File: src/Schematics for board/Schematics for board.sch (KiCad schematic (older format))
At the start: 1 part

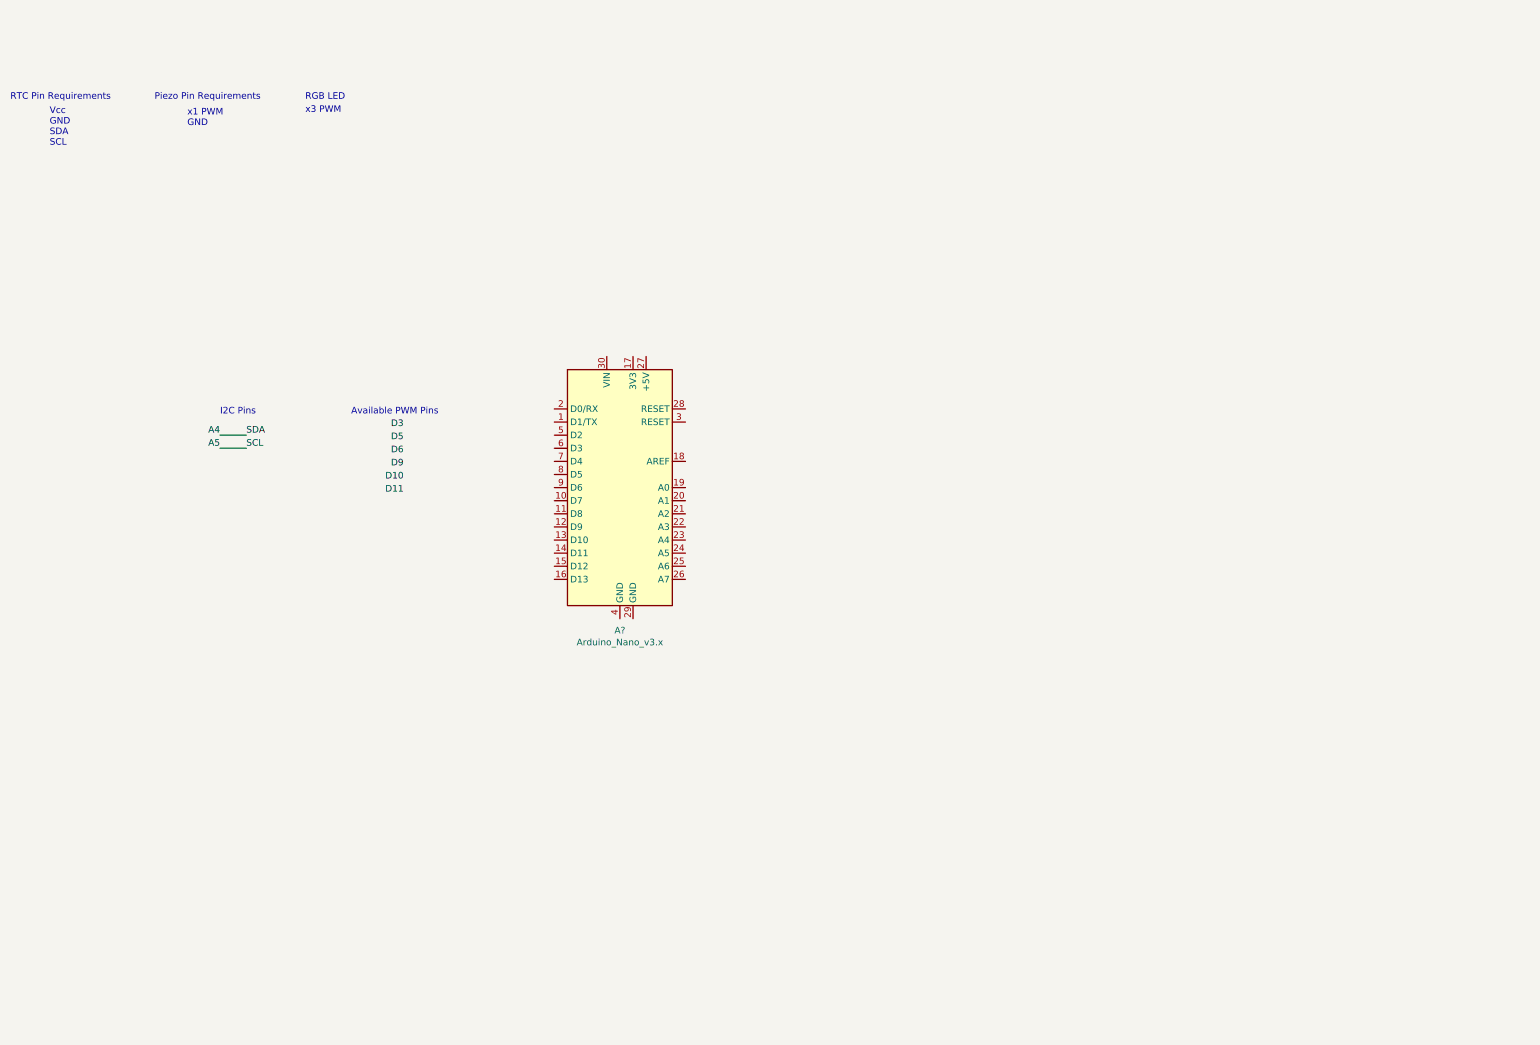
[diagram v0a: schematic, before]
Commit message: Rev1.0 of Board layout
Rev1 of how each part is going to be connected in out board
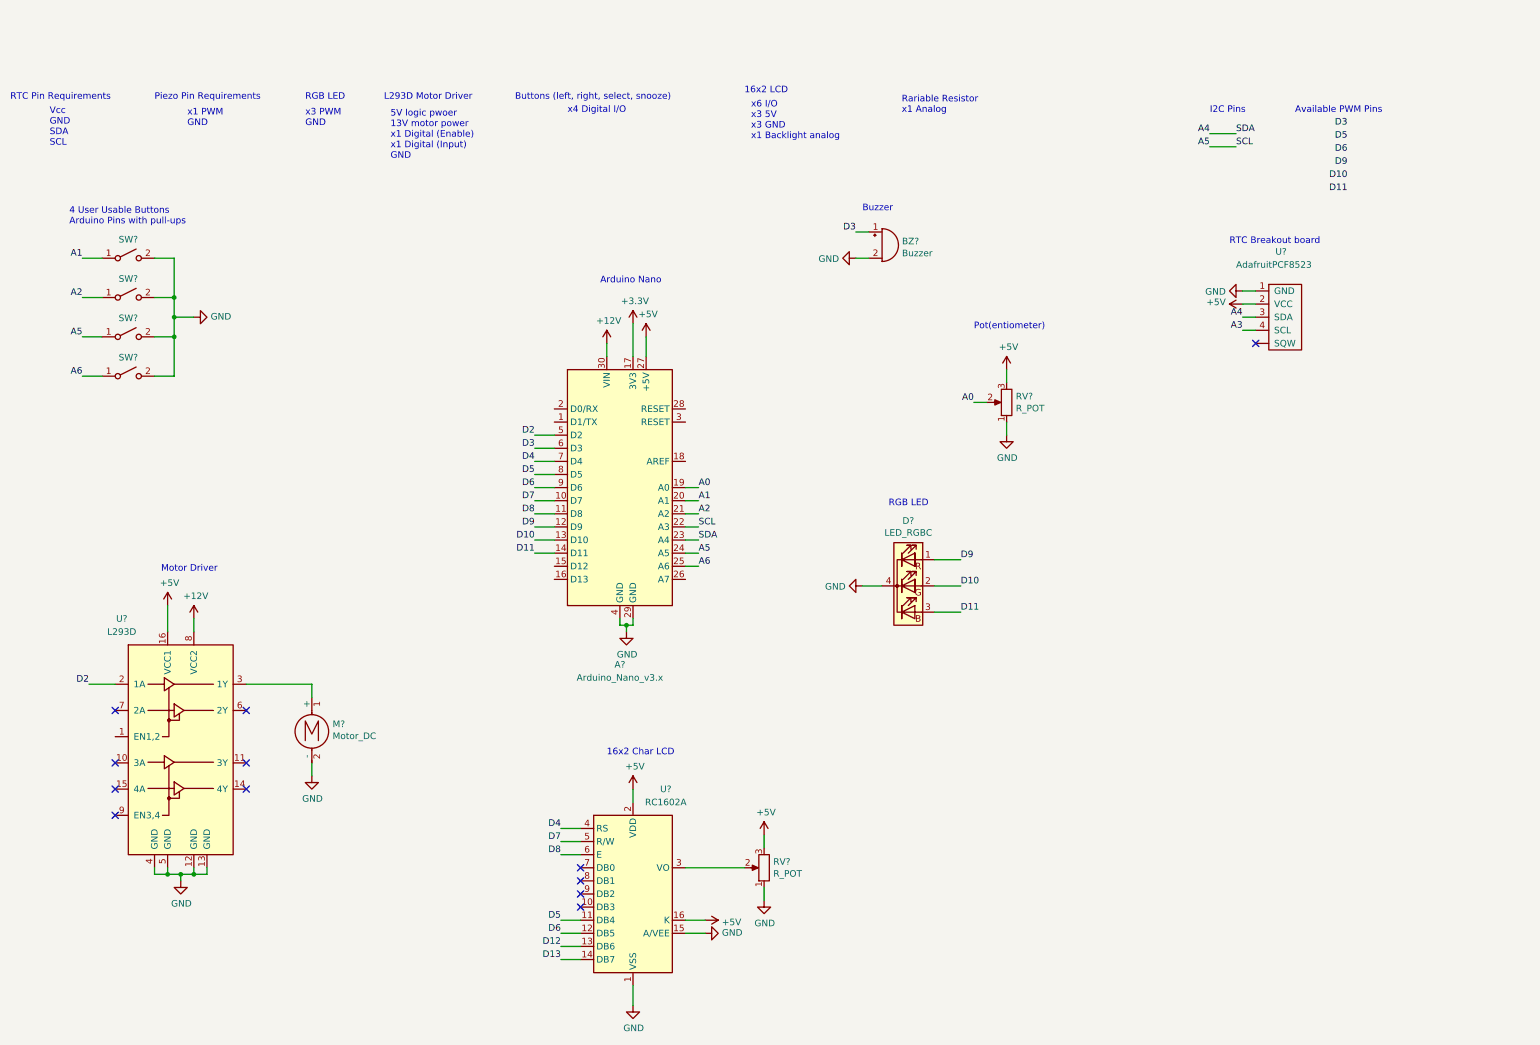
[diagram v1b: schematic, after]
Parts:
- added BZ?: Buzzer, symbol Device:Buzzer
- added D?: LED_RGBC, symbol Device:LED_RGBC
- added M?: Motor_DC, symbol Motor:Motor_DC
- added RV? (x2): R_POT, symbol Device:R_POT
- added SW? (x4): ~, symbol Switch:SW_SPST
- added U?: AdafruitPCF8523, symbol Timer_RTC:AdafruitPCF8523
- added U?: L293D, Package_DIP:DIP-16_W7.62mm, symbol Driver_Motor:L293D
- added U?: RC1602A, Display:RC1602A, symbol Display_Character:RC1602A
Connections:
- net A4: now also A?.23 (A4), U?.3 (SDA)
- net A5: now also A?.22 (A3), A?.24 (A5), SW?.1 (A)
- net D10: now also A?.13 (D10), D?.2 (GA)
- net D11: now also A?.14 (D11), D?.3 (BA)
- net D3: now also A?.6 (D3), BZ?.1 (-)
- net D5: now also A?.8 (D5), U?.11 (DB4)
- net D6: now also A?.9 (D6), U?.12 (DB5)
- net D9: now also A?.12 (D9), D?.1 (RA)
- net D7: now reaches A?.10 (D7)
- net D7: now also U?.5 (R/W)
- net D8: now reaches A?.11 (D8)
- net D8: now also U?.6 (E)
- net +3V3: now reaches A?.17 (3V3)
- net A0: now reaches A?.19 (A0)
- net A0: now also RV?.2
- net A1: now reaches A?.20 (A1)
- net A1: now also SW?.1 (A)
- net A2: now reaches A?.21 (A2)
- net A2: now also SW?.1 (A)
- net A6: now reaches A?.25 (A6)
- net A6: now also SW?.1 (A)
- net +5V: now reaches A?.27 (+5V)
- net +5V: now also RV?.3, RV?.3, U?.16 (K), U?.16 (VCC1), U?.2 (VCC), U?.2 (VDD)
- net GND: now reaches A?.29 (GND)
- net GND: now also A?.4 (GND), BZ?.2 (+), D?.4 (K), M?.2 (-), RV?.1, RV?.1, SW?.2 (B), SW?.2 (B), SW?.2 (B), SW?.2 (B), U?.1 (GND), U?.1 (VSS), U?.12 (GND), U?.13 (GND), U?.15 (A/VEE), U?.4 (GND), U?.5 (GND)
- net +12V: now reaches A?.30 (VIN)
- net +12V: now also U?.8 (VCC2)
- net D2: now reaches A?.5 (D2)
- net D2: now also U?.2 (1A)
- net D4: now reaches A?.7 (D4)
- net D4: now also U?.4 (RS)
- new net: M?.1 (+), U?.3 (1Y)
- new net: RV?.2, U?.3 (VO)
- new net A3: U?.4 (SCL)
- new net D12: U?.13 (DB6)
- new net D13: U?.14 (DB7)
- no-connect marks 0 -> 12
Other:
- note added: "16x2 Char LCD"
- note added: "16x2 LCD"
- note added: "4 User Usable Buttons\nArduino Pins with pull-ups"
- note added: "5V logic pwoer\n13V motor power\nx1 Digital (Enable)\nx1 Digital (Input)\nGND\n"
- note added: "Arduino Nano"
- note added: "Buttons (left, right, select, snooze)"
- note added: "Buzzer"
- note added: "L293D Motor Driver"
- note added: "Motor Driver"
- note added: "Pot(entiometer)"
- note added: "RGB LED\n"
- note added: "RTC Breakout board"
- note added: "Rariable Resistor\nx1 Analog"
- note added: "x3 PWM\nGND"
- note added: "x4 Digital I/O"
- note added: "x6 I/O\nx3 5V\nx3 GND\nx1 Backlight analog"
- note removed: "x3 PWM"

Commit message: updated schematic and LCD code
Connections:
- net D13 is gone; now on net D7: U?.14 (DB7)
- net D12: now also A?.15 (D12)
- net D7: no longer A?.10 (D7), U?.5 (R/W)
- net GND: now also U?.5 (R/W)
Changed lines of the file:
@@
 Wire Wire Line
 	4600 3400 4750 3400
-Text Label 4800 6300 2    50   ~ 0
-D7
-Wire Wire Line
-	4800 6300 4950 6300
-Text Label 4600 3700 2    50   ~ 0
-D7
-Wire Wire Line
-	4600 3700 4750 3700
 Text Notes 5150 5650 0    50   ~ 0
 16x2 Char LCD
@@
 Text Notes 7950 2400 0    50   ~ 0
 Pot(entiometer)
-Text Notes 9900 1750 0    50   ~ 0
+Text Notes 11300 50   0    50   ~ 0
 RTC Breakout board
 Text Notes 1750 4250 0    50   ~ 0
@@
 Text Label 4800 7100 2    50   ~ 0
 D12
-Text Label 4800 7200 2    50   ~ 0
-D13
 NoConn ~ 4950 6500
 NoConn ~ 4950 6600
@@
 Text Notes 7300 3750 0    50   ~ 0
 RGB LED\n
+$Comp
+L power:GND #PWR?
+U 1 1 5E2C8739
+P 4700 6300
+F 0 "#PWR?" H 4700 6050 50  0001 C CNN
+F 1 "GND" V 4705 6172 50  0000 R CNN
+F 2 "" H 4700 6300 50  0001 C CNN
+F 3 "" H 4700 6300 50  0001 C CNN
+	1    4700 6300
+	0    1    1    0
+$EndComp
+Wire Wire Line
+	4700 6300 4950 6300
+Text Label 4800 7200 2    50   ~ 0
+D7
+Text Label 4600 3700 2    50   ~ 0
+D7
+Text Label 4600 4200 2    50   ~ 0
+D12
+Wire Wire Line
+	4600 4200 4750 4200
 $EndSCHEMATC

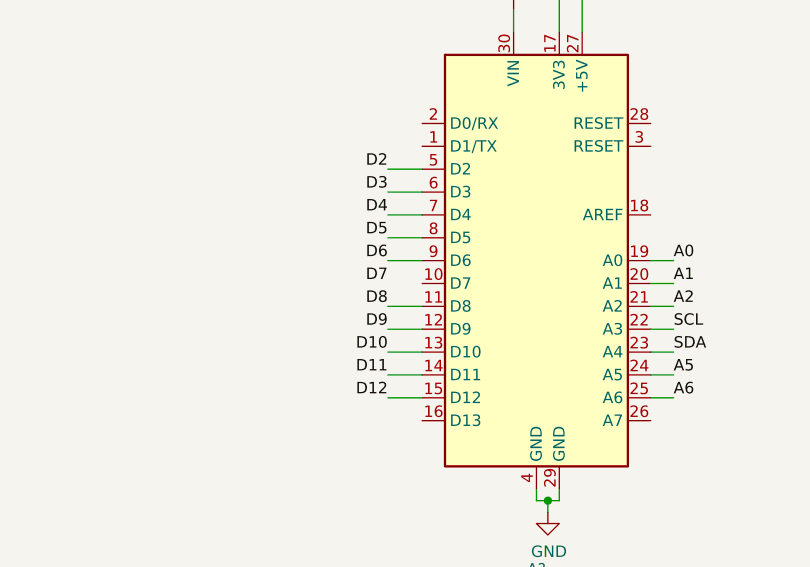
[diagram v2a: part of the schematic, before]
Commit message: small updates to motor code
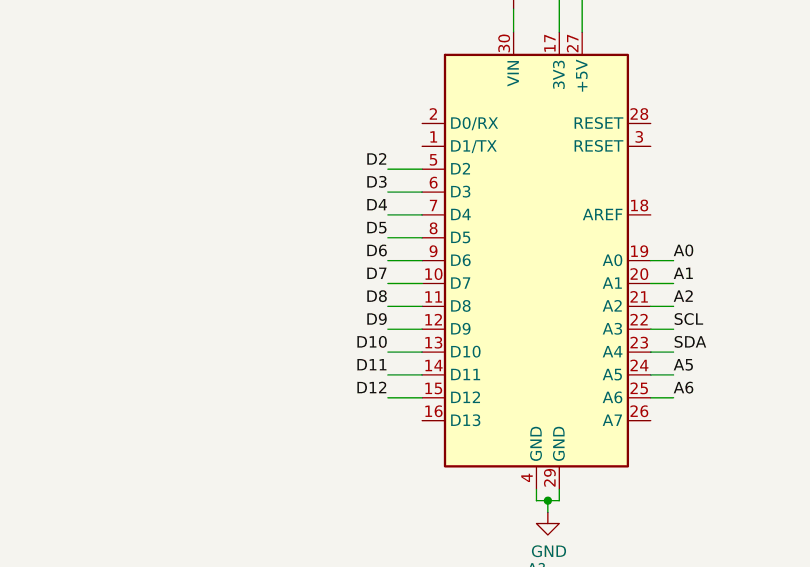
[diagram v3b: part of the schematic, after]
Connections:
- net D7: now also A?.10 (D7)
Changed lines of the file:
@@
 EESchema Schematic File Version 4
+LIBS:Schematics for board-cache
 EELAYER 30 0
 EELAYER END
@@
 Wire Wire Line
 	4600 4200 4750 4200
+Wire Wire Line
+	4600 3700 4750 3700
 $EndSCHEMATC
